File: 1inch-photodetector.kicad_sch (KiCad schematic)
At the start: 23 parts, among them J1 Conn_01x03, J2 Conn_Coaxial, U1 ADA4898-2, U2 LT3032IDE-12

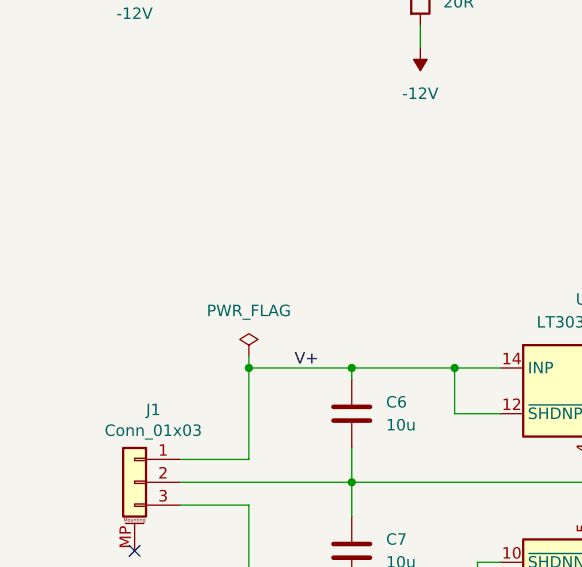
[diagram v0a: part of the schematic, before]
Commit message: Fix missing soldermask cutout around PD
- Bump KiCad to version 10
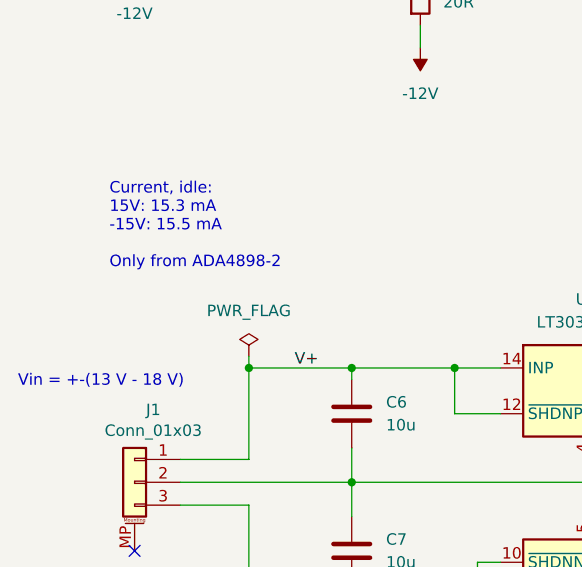
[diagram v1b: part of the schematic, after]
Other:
- note added: "Current, idle: 15V: 15.3 mA -15V: 15.5 mA Only from ADA4898-2"
- note added: "Vin = +-(13 V - 18 V)"
